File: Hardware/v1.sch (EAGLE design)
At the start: 33 parts, among them IC1 IC_FT2232H-56Q, IC3 IC_MAX3313, X1 6MHz

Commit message: added eeprom and expanded sch
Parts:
- added C13: 100nF, rcl:C-EUC0603
- added C14: 10uF, rcl:C-EUC0603
- added CN1: (no value), m0wut:USBMUSB
- added IC2: 93LC46AT-I/OT, Microchip_By_element14_Batch_1:93LC46AT-I/OT
- C3, C4, C5: device rcl:C-EUC0805 -> rcl:C-EUC0603
- LD1, LD2: device adafruit:LEDCHIP-LED0603 -> adafruit:LED3MM
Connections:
- net CAT_RX renamed UART(K3_TO_PIC)
- net N$4 renamed RS232(PIC_TO_K3)
- net N$5 renamed RS232(K2_TO_PIC)
- removed net N$20: IC1.EEDATA, R12.2
- new net N$28: IC2.DO, R12.1
- new net UART(CAT_TO_USB): R6.2
- new net UART(PIC_TO_K3): IC3.TIN
- new net UART(USB_TO_CAT): R5.2
- new net UART(USB_TO_WK): R7.2
- new net UART(WK_TO_USB): R8.2
- new net USB_N: CN1.D-, R3.1
- new net USB_P: CN1.D+, R4.1
- new net VCC: CN1.VBUS
- net +3V3: now also C13.1, C14.1, IC2.VCC
- net GND: now also C13.2, C14.2, CN1.GND, IC2.VSS
- net N$18: now also IC2.CS
- net N$19: now also IC2.CLK
- net N$21: now also IC1.EEDATA, IC2.DI, R12.2; no longer R12.1
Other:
- note added: "KIO3_USB"
- note added: "PIC"
- note added: "RS232 Converter"
- note added: "USB Interface"
- note removed: "WINK3Y Nano"

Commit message: Resized PCB now I have reference board
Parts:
- removed C10, C11, C12, C13, C9: 100nF, rcl:C-EUC0603
- removed FB1, FB2: FB0603, rcl:FB0603
- removed IC2: 93LC46AT-I/OT, Microchip_By_element14_Batch_1:93LC46AT-I/OT
- removed LD1, LD2: (no value), adafruit:LED3MM
- removed R10, R11, R9: 10k, rcl:R-EU_R0603
- removed R12: 2k2, rcl:R-EU_R0603
- removed R13, R14, R5, R6, R7, R8: (no value), rcl:R-EU_R0603
- removed R3: 27R, rcl:R-EU_R0603
- removed X1: 6MHz, m0wut:XTAL_MURATA_3-PIN-RES
- added C15: 22pF, rcl:C-EUC0603
- added CAN1: CAN_LAIRD-BMI-S-203-F, m0wut:CAN_LAIRD-BMI-S-203-F
- added CN2: TSW-120-08-L-S-RA, m0wut:CONN_0.1"_1X20
- added CN3: CONN_TE_DB9, m0wut:CONN_TE_DB9
- added CN4: CONN_TE_DB-HD15, m0wut:CONN_TE_DB-HD15
- added Q1: (no value), adafruit:CRYSTALHC49UP
- added R17: 1k5, rcl:R-EU_R0603
- added U1: TUSB2036VF, Texas Instruments_By_element14_Batch_1:TUSB2036VF
- C1, C2, C6, C8: value 100nF -> 1uF
- C14: value 10uF -> 22pF
- C7: value 3.3uF -> 1uF
- CN1: value (none) -> 629105150521; device m0wut:USBMUSB -> m0wut:USBWURTH
- IC1: value IC_FT2232H-56Q -> ADUM3160BRWZ; device m0wut:IC_FT2232H-56Q -> m0wut:ADUM3160BRWZ
- R1: value 12k -> 24; device rcl:R-EU_R0603 -> rcl:R-EU_R0402
- R2: value 1k -> 24; device rcl:R-EU_R0603 -> rcl:R-EU_R0402
- R4: value 27R -> 15k
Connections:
- removed net +1V8: C10.1, C7.1, C9.1, IC1.VCORE, IC1.VREGOUT
- removed net N$12: C11.1, FB2.2, IC1.VPHY
- removed net N$13: C12.1, FB1.2, IC1.VPLL
- removed net N$14: IC1.ADBUS0, R5.1
- removed net N$15: IC1.ADBUS1, R6.1
- removed net N$16: IC1.BDBUS0, R7.1
- removed net N$17: IC1.BDBUS1, R8.1
- removed net N$18: IC1.EECS, IC2.CS, R9.1
- removed net N$19: IC1.EECLK, IC2.CLK, R10.1
- removed net N$21: IC1.EEDATA, IC2.DI, R11.1, R12.2
- removed net N$22: IC1.ACBUS1, IC1.ACBUS2, R13.1
- removed net N$23: IC1.BCBUS3, IC1.BCBUS4, R14.1
- removed net N$24: LD1.C, R13.2
- removed net N$25: LD2.C, R14.2
- removed net N$28: IC2.DO, R12.1
- removed net UART(CAT_TO_USB): R6.2
- removed net UART(USB_TO_CAT): R5.2
- removed net UART(USB_TO_WK): R7.2
- removed net UART(WK_TO_USB): R8.2
- removed net USB_N: CN1.D-, R3.1
- removed net USB_P: CN1.D+, R4.1
- removed net VCC: CN1.VBUS
- new net AGND: C1.2, C2.2, CN1.GND, IC1.GND1, IC1.GND1_2
- new net DM0: IC1.DD-, U1.DM0
- new net DM1: U1.DM1
- new net DM2: U1.DM2
- new net DM3: U1.DM3
- new net DP0: IC1.DD+, U1.DP0
- new net DP0PUR: U1.DP0PUR
- new net DP1: U1.DP1
- new net DP2: U1.DP2
- new net DP3: U1.DP3
- new net N$4: IC1.UD+, R1.2
- new net N$5: C1.1, CN1.VBUS, IC1.VBUS1
- new net XTAL1: C14.1, Q1.1, U1.XTAL1/CLK48
- new net XTAL2: R17.2, U1.XTAL2
- net +3V3: now also C7.1, IC1.PIN, IC1.SPD, IC1.VBUS2, IC1.VDD2, R4.1, U1.VCC, U1.VCC_2, U1.~BUSPWR, U1.~EXTMEM, U1.~NP3, U1.~OVRCUR1, U1.~OVRCUR2, U1.~OVRCUR3; no longer C1.1, C13.1, C14.1, C2.1, C6.1, FB1.1, FB2.1, IC1.VCCIO, IC1.VREGIN, IC2.VCC, LD1.A, LD2.A, R10.2, R11.2, R2.1, R9.2
- net GND: now also C15.2, C6.1, CAN1.P$1, IC1.GND2, IC1.GND2_2, U1.EEDATA/~GANGED, U1.GND, U1.GND_2, U1.MODE, U1.NPINT0, U1.NPINT1, U1.~OCPROT/~PWRSW; no longer C1.2, C10.2, C11.2, C12.2, C13.2, C2.2, C6.2, C9.2, CN1.GND, IC1.GND, IC1.TEST, IC2.VSS, R1.1, X1.CAN
- net N$1: now also CN1.D+, R1.1; no longer IC1.OSCI, X1.XTAL2
- net N$10: now also C6.2, R4.2, U1.~RESET; no longer IC1.DM, R3.2
- net N$11: now also C15.1, Q1.2, R17.1; no longer IC1.DP, R4.2
- net N$2: now also CN1.D-, R2.1; no longer IC1.OSCO, X1.XTAL1
- net N$3: now also IC1.UD-, R2.2; no longer IC1.REF, R1.2
- net N$9: now also C2.1, IC1.PDEN, IC1.SPU, IC1.VDD1; no longer IC1.RESET, R2.2
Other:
- note added: "Connectors"

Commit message: finished input side of usb isolator
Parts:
- removed CAN1: CAN_LAIRD-BMI-S-203-F, m0wut:CAN_LAIRD-BMI-S-203-F
- removed Q1: (no value), adafruit:CRYSTALHC49UP
- removed R17: 1k5, rcl:R-EU_R0603
- removed U1: TUSB2036VF, Texas Instruments_By_element14_Batch_1:TUSB2036VF
- added C10, C11: 100nF, rcl:C-EUC0603
- added C12, C13, C16, C17, C18, C19, C20, C21, C22, C23, C24: 1nF, rcl:C-EUC0603
- added C9: 1uF, rcl:C-EUC0603
- added D1: D_ST_USBULC6, m0wut:D_ST_USBULC6
- added IC2: TUSB2046BIRHBT, texas:TUSB2046BIRHBIRHB
- added R10, R11, R12, R13, R6, R7, R8, R9: 24, rcl:R-EU_R0402
- added R3: 24, rcl:R-EU_R0603
- added R5: 15k, rcl:R-EU_R0603
- C14, C15: value 22pF -> 1nF
- CN3: value CONN_TE_DB9 -> 1734354-1
- CN4: value CONN_TE_DB-HD15 -> 1-1734530-1
- R4: value 15k -> 24
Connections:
- removed net DP0PUR: U1.DP0PUR
- removed net XTAL1: C14.1, Q1.1, U1.XTAL1/CLK48
- removed net XTAL2: R17.2, U1.XTAL2
- new net 6MHZ_HUB: IC2.XTAL1
- new net D+: D1.LEFT, IC1.UD+, R1.2
- new net D-: D1.RIGHT, IC1.UD-, R2.2
- new net DM4: R7.2
- new net DP4: R6.2
- new net N$12: IC2.DM1, R8.2
- new net N$13: IC2.DP1, R9.2
- new net N$14: IC2.DM2, R10.2
- new net N$15: IC2.DP2, R11.2
- new net N$16: IC2.DP3, R12.1
- new net N$17: IC2.DM3, R13.1
- new net N$18: C23.1, CN4.14
- new net N$19: CN4.12
- new net N$20: CN4.5
- new net N$21: C24.1, CN4.15
- new net N$22: C22.1, CN4.13
- new net N$23: C21.1, CN4.11
- new net N$24: C20.1, CN4.10
- new net N$25: C19.1, CN4.9
- new net N$26: C18.1, CN4.8
- new net N$27: C17.1, CN4.7
- new net N$28: C16.1, CN4.6
- new net N$29: C15.1, CN4.4
- new net N$30: C14.1, CN4.3
- new net N$31: C13.1, CN4.2
- new net N$32: C12.1, CN4.1
- new net VCC: C1.1, CN1.VBUS, D1.V+, IC1.VBUS1
- net +3V3: now also C10.1, C11.1, C6.1, C9.1, IC2.!EXTMEM, IC2.VCC, IC2.VCC@1, R5.1; no longer C8.1, R4.1, U1.VCC, U1.VCC_2, U1.~BUSPWR, U1.~EXTMEM, U1.~NP3, U1.~OVRCUR1, U1.~OVRCUR2, U1.~OVRCUR3
- net AGND: now also C12.2, C13.2, C14.2, C15.2, C16.2, C17.2, C18.2, C19.2, C20.2, C21.2, C22.2, C23.2, C24.2, CN3.TAB, CN4.TAB, D1.GND
- net DM0: now also IC2.DM0, R3.2; no longer IC1.DD-, U1.DM0
- net DM1: now also R8.1; no longer U1.DM1
- net DM2: now also R10.1; no longer U1.DM2
- net DM3: now also R13.2; no longer U1.DM3
- net DP0: now also IC2.DP0, R4.2; no longer IC1.DD+, U1.DP0
- net DP1: now also R9.1; no longer U1.DP1
- net DP2: now also R11.1; no longer U1.DP2
- net DP3: now also R12.2; no longer U1.DP3
- net GND: now also C10.2, C11.2, C6.2, C9.2, CN3.5, IC2.BUSPWR, IC2.EEDATA/GANGED, IC2.GND, IC2.GND@1, IC2.PAD, IC2.TSTMODE, IC2.TSTPLL/48MCLK; no longer C14.2, C15.2, C6.1, CAN1.P$1, U1.EEDATA/~GANGED, U1.GND, U1.GND_2, U1.MODE, U1.NPINT0, U1.NPINT1, U1.~OCPROT/~PWRSW
- net N$10: now also IC1.DD-, R3.1; no longer C6.2, R4.2, U1.~RESET
- net N$11: now also IC1.DD+, R4.1; no longer C15.1, Q1.2, R17.1
- net N$3: now also C8.1, IC2.!RESET, R5.2; no longer IC1.UD-, R2.2
- net N$4: now also IC2.DP4, R6.1; no longer IC1.UD+, R1.2
- net N$5: now also IC2.DM4, R7.1; no longer C1.1, CN1.VBUS, IC1.VBUS1

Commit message: most of usb hub implemented
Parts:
- added C25, C27, C28: 100nF, rcl:C-EUC0402
- added C26: 33nF, rcl:C-EUC0402
- added IC4: FT2232D, ftdichip-3:FT2232D
- added IC6: PCM2903C, texas:PCM2902E
- added R14: 1k5, rcl:R-EU_R0402
- added R15: 470, rcl:R-EU_R0402
- added R16: 10k, rcl:R-EU_R0402
- C1, C10, C11, C2, C6, C7, C8, C9: device rcl:C-EUC0603 -> rcl:C-EUC0402
- R3, R4, R5: device rcl:R-EU_R0603 -> rcl:R-EU_R0402
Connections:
- new net 6MHZ_FT: IC4.XTIN
- new net CAT_232_TO_PIC: IC4.ADBUS0
- new net CAT_PIC_TO_232: IC4.ADBUS1
- new net N$33: C27.1, IC4.AVCC, R15.1
- new net N$37: IC4.EEDATA, R16.2
- new net VDD: C26.1, IC4.3V3OUT, R14.1
- new net WK_232_TO_PIC: IC4.BDBUS0
- new net WK_PIC_TO_232: IC4.BDBUS1
- net +5V: now also C25.1, C28.1, IC4.-RESET, IC4.SI/WUA, IC4.SI/WUB, IC4.VCC@1, IC4.VCC@2, IC4.VCCIOA, IC4.VCCIOB, R15.2, R16.1
- net DM2: now also IC4.D-
- net DM4: now also IC6.D-
- net DP2: now also IC4.D+, R14.2
- net DP4: now also IC6.D+
- net GND: now also C25.2, C26.2, C27.2, C28.2, IC4.AGND, IC4.GND@1, IC4.GND@2, IC4.GND@3, IC4.GND@4, IC4.TEST
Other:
- note added: "TO CODEC"
- note added: "TO FT2232"

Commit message: mirrored digital section of board to allow for easier routing to io
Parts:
- removed R12, R13, R8, R9: 24, rcl:R-EU_R0402
- added L1: 100uH, m0wut:INDUCTOR
- added R17, R18, R19, R20, R21, R22, R23, R24, R25, R26, R27, R28: 220, rcl:R-EU_R0805
- added R29: 137k, rcl:R-EU_R0805
- C12, C13, C14, C15, C16, C17, C18, C19, C20, C21, C22, C23, C24: device rcl:C-EUC0603 -> rcl:C-EUC0402
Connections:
- net N$4 renamed USB4_P
- net N$5 renamed USB4_N
- removed net DM1: R8.1
- removed net DM3: R13.2
- removed net DP1: R9.1
- removed net DP3: R12.2
- removed net N$18: C23.1, CN4.14
- removed net N$19: CN4.12
- removed net N$20: CN4.5
- removed net N$21: C24.1, CN4.15
- removed net N$22: C22.1, CN4.13
- removed net N$23: C21.1, CN4.11
- removed net N$24: C20.1, CN4.10
- removed net N$25: C19.1, CN4.9
- removed net N$26: C18.1, CN4.8
- removed net N$27: C17.1, CN4.7
- removed net N$28: C16.1, CN4.6
- removed net N$29: C15.1, CN4.4
- removed net N$30: C14.1, CN4.3
- removed net N$31: C13.1, CN4.2
- removed net N$32: C12.1, CN4.1
- new net 232_COM: CN2.P$1
- new net 232_DTR: CN2.P$2
- new net 232_RTS: CN2.P$4
- new net 232_RXD: CN2.P$5
- new net 232_TXD: CN2.P$3
- new net 5V_IN: CN2.P$20
- new net ACC_ALC: CN2.P$12, R29.1
- new net ACC_AUX: CN2.P$15, R18.1
- new net ACC_BND0: CN2.P$7, R27.1
- new net ACC_BND1: CN2.P$14, R19.1
- new net ACC_BND2: CN2.P$9, R24.1
- new net ACC_BND3: CN2.P$8, R28.1
- new net ACC_COM: CN2.P$6
- new net ACC_COMMON: CN4.12, CN4.5, L1.2
- new net ACC_DI0: CN2.P$16, R17.1
- new net ACC_DI1: CN2.P$17, R22.1
- new net ACC_DO0: CN2.P$18, R21.1
- new net ACC_DO1: CN2.P$19, R26.1
- new net ACC_KEY: CN2.P$10, R25.1
- new net ACC_PTT: CN2.P$13, R20.1
- new net ACC_PWR: CN2.P$11, R23.1
- new net ALC_X: C24.1, CN4.15, R29.2
- new net AUX_X: C13.1, CN4.2, R18.2
- new net BND0_X: C22.1, CN4.13, R27.2
- new net BND1_X: C14.1, CN4.3, R19.2
- new net BND2_X: C19.1, CN4.9, R24.2
- new net BND3_X: C23.1, CN4.14, R28.2
- new net DIG0_X: C12.1, CN4.1, R17.2
- new net DIG1_X: C17.1, CN4.7, R22.2
- new net DIGO1_X: C21.1, CN4.11, R26.2
- new net DIGO_X: C16.1, CN4.6, R21.2
- new net KEY_X: C20.1, CN4.10, R25.2
- new net PTT_X: C15.1, CN4.4, R20.2
- new net PWR_X: C18.1, CN4.8, R23.2
- net GND: now also L1.1
- net N$12: no longer R8.2
- net N$13: no longer R9.2
- net N$16: no longer R12.1
- net N$17: no longer R13.1
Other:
- note added: "Audio Codec"
- note added: "FT2232"
- note added: "USB Hub"
- note added: "USB Input"
- note added: "USB0 (Not Used)"
- note added: "USB3 (Not Used)"
- note removed: "USB Interface"

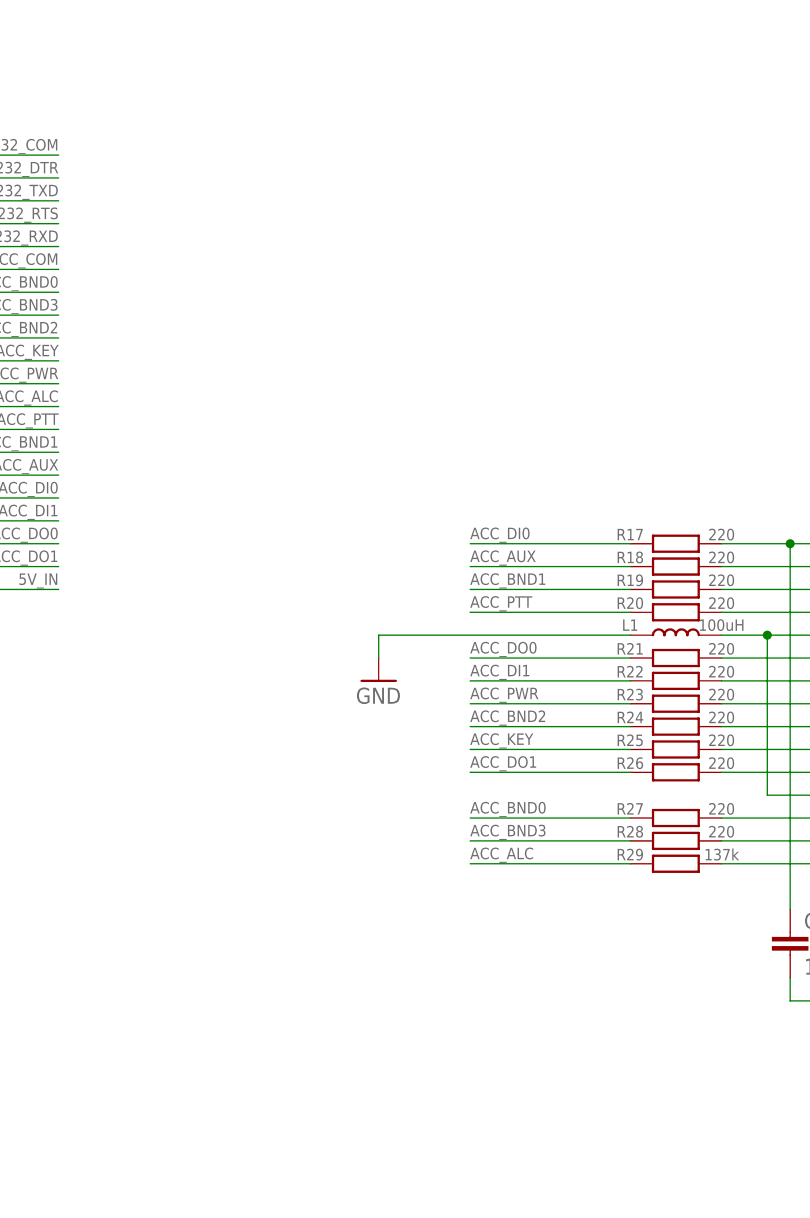
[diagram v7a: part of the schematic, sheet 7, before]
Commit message: added missing pullups to band lines
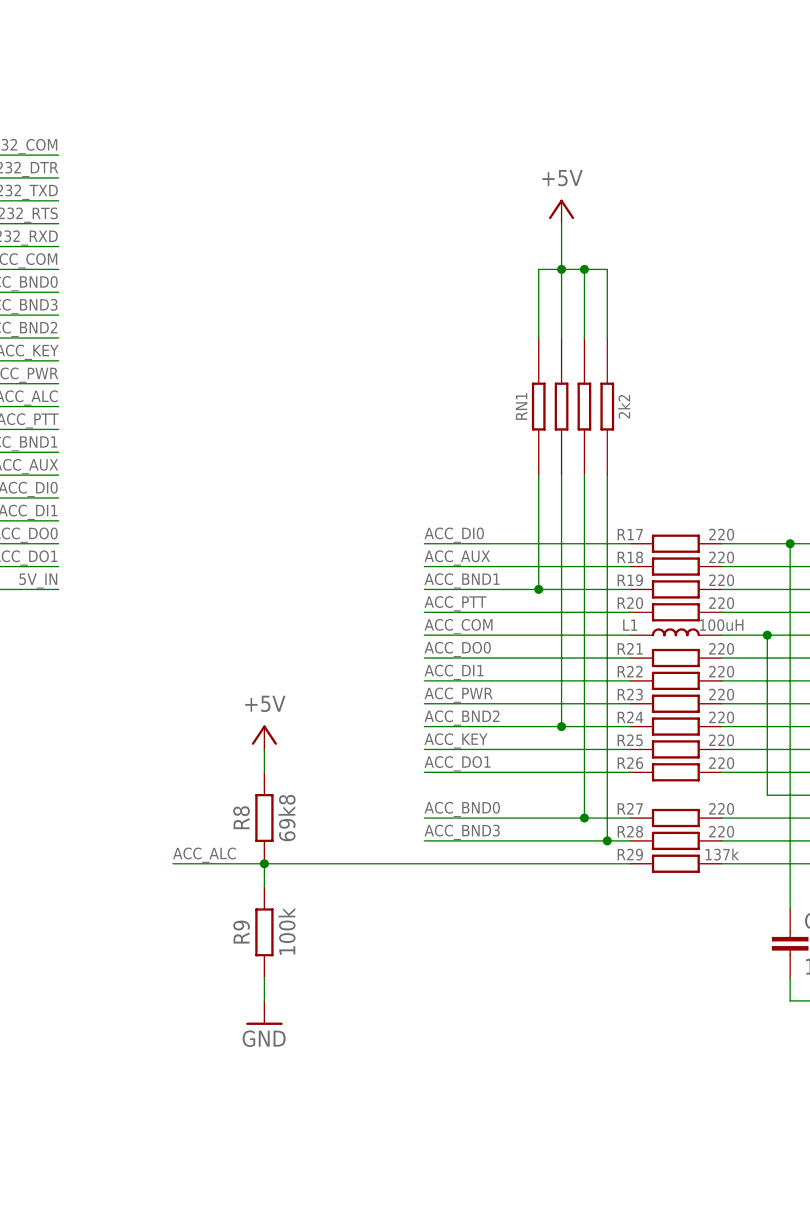
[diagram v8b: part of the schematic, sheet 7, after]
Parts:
- added C29: 100nF, rcl:C-EUC0402
- added C30: 1uF, rcl:C-EUC0402
- added R8: 69k8, rcl:R-EU_R0603
- added R9: 100k, rcl:R-EU_R0603
- added RN1: 2k2, m0wut:R_BOURNS_CAY16-J4
- C7: value 1uF -> 100nF
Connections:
- net +5V: now also C29.1, C30.1, R8.2, RN1.1, RN1.2, RN1.3, RN1.4
- net ACC_ALC: now also R9.2
- net ACC_BND0: now also RN1.3A
- net ACC_BND1: now also RN1.1A
- net ACC_BND2: now also RN1.2A
- net ACC_BND3: now also RN1.4A
- net ACC_COM: now also L1.1
- net GND: now also C29.2, C30.2, R9.1; no longer L1.1
